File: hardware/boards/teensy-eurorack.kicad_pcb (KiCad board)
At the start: 2 copper layers, 118.1 x 101.6 mm, 98 parts, among them J10 AudioJack3_SwitchTR, J27 Conn_01x02, J28 Conn_02x08_Odd_Even, J4 AudioJack3_SwitchTR, J5 AudioJack3_SwitchTR, J6 AudioJack3_SwitchTR, J7 AudioJack3_SwitchTR, J8 AudioJack3_SwitchTR, J9 AudioJack3_SwitchTR, U1 CS42448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

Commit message: pcboard: re-connect LRCLK to codec, move hole for sd-extender cable further away from teensy, and move usb B headers up to avoid collision with SD-extender
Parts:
- moved JUSBB1 10.8 mm to (195.6, 116.8)
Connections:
- J10 pad RN: (no net) -> Net-(J10-PadRN)
- J10 pad TN: (no net) -> Net-(J10-PadTN)
- J28 pad 13: (no net) -> Net-(J28-Pad13)
- J28 pad 14: (no net) -> Net-(J28-Pad14)
- J28 pad 15: (no net) -> Net-(J28-Pad15)
- J28 pad 16: (no net) -> Net-(J28-Pad16)
- J4 pad RN: (no net) -> Net-(J4-PadRN)
- J4 pad TN: (no net) -> Net-(J4-PadTN)
- J5 pad RN: (no net) -> Net-(J5-PadRN)
- J5 pad TN: (no net) -> Net-(J5-PadTN)
- J6 pad RN: (no net) -> Net-(J6-PadRN)
- J6 pad TN: (no net) -> Net-(J6-PadTN)
- JM1 pad 5: (no net) -> Net-(JM1-Pad5)
- JM1 pad 6: (no net) -> Net-(JM1-Pad6)
- JM1 pad 7: (no net) -> Net-(JM1-Pad7)
- U1 pad 11: (no net) -> Net-(U1-Pad11)
- U1 pad 12: (no net) -> Net-(U1-Pad12)
- U1 pad 19: GND -> /LRCLK
- U1 pad 20: (no net) -> Net-(U1-Pad20)
- U1 pad 21: (no net) -> Net-(U1-Pad21)
- U1 pad 25: (no net) -> Net-(U1-Pad25)
- U1 pad 28: (no net) -> Net-(U1-Pad28)
- U1 pad 29: (no net) -> Net-(U1-Pad29)
- U1 pad 32: (no net) -> Net-(U1-Pad32)
- U1 pad 33: (no net) -> Net-(U1-Pad33)
- U1 pad 35: (no net) -> Net-(U1-Pad35)
- U1 pad 37: (no net) -> Net-(U1-Pad37)
- U1 pad 38: (no net) -> Net-(U1-Pad38)
- U1 pad 41: (no net) -> Net-(U1-Pad41)
- U1 pad 5: GND -> /LRCLK
- U1 pad 57: (no net) -> Net-(U1-Pad57)
- U1 pad 59: (no net) -> Net-(U1-Pad59)
- U1 pad 61: (no net) -> Net-(U1-Pad61)
- U4 pad 15: (no net) -> Net-(U4-Pad15)
- U4 pad 24: (no net) -> Net-(U4-Pad24)
- U4 pad 25: (no net) -> Net-(U4-Pad25)
- U4 pad 27: (no net) -> Net-(U4-Pad27)
- U4 pad 30: (no net) -> Net-(U4-Pad30)
- U4 pad 31: (no net) -> Net-(U4-Pad31)
- U4 pad 32: (no net) -> Net-(U4-Pad32)
- U4 pad 42: (no net) -> /LRCLK
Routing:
- net /LRCLK: track 0.00 -> 98.8 mm, vias 0 -> 2
- net Net-(JMUSBB1-Pad3): track 93.6 -> 80.1 mm
- net Net-(JMUSBB1-Pad4): track 96.6 -> 84.9 mm
- net Net-(JMUSBB1-Pad2): track 92.7 -> 82.0 mm
- net Net-(J27-Pad2): track 17.9 -> 21.6 mm
- net +3V3: track 277.0 -> 274.1 mm, vias 8 -> 9
- net /BCLK: track 85.3 -> 86.9 mm
- net /SDA: track 72.2 -> 71.1 mm
- net /SCL: track 73.2 -> 72.4 mm
- net /MCLK: track 79.7 -> 80.2 mm
- net /TDM_OUT: track 68.7 -> 68.2 mm
- net GND: track 145.8 -> 146.0 mm, vias 88 -> 98
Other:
- outline, holes or cut-outs redrawn
- board text added: "Teensy eurorack audio shield 9 Aug 2020 v1.9.1b"
- board text added: "https://github.com/newdigate/teensy-eurorack version 1.9.1b"
- board text removed: "Teensy eurorack audio shield 26 July 2020 v1.9.1"
- board text removed: "https://github.com/newdigate/teensy-eurorack version 1.9.1"

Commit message: silkscreen improvements
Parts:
- FB1: value Ferrite_Bead -> 220
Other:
- board text added: "Eurorack power bus"
- board text added: "USB device connection (to host) using female USB-B socket on front panel"
- board text added: "USB host connection using USB-A female socket on front panel"
- board text added: "connect jumper J27 to power from eurorack power bus 5v CAUTION: Do not connect teensy to host while using eurorack power."
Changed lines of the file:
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@@
   (general
     (thickness 1.6)
-    (drawings 23)
+    (drawings 35)
     (tracks 1524)
     (zones 0)
@@
   )
   (setup
-    (last_trace_width 0.4064)
+    (last_trace_width 0.2286)
     (user_trace_width 0.1524)
     (user_trace_width 0.2286)
@@
     (descr "Through hole straight pin header, 1x04, 2.54mm pitch, single row")
     (tags "Through hole pin header THT 1x04 2.54mm single row")
-    (fp_text reference JUSBB1 (at 0 2.33 -90) (layer B.SilkS)
+    (fp_text reference JUSBB1 (at 0 2.33 -90) (layer B.SilkS) hide
       (effects (font (size 1 1) (thickness 0.15)) (justify mirror))
     )
@@
     (descr "Through hole straight pin header, 2x08, 2.54mm pitch, double rows")
     (tags "Through hole pin header THT 2x08 2.54mm double row")
-    (fp_text reference J28 (at 1.27 2.33) (layer B.SilkS)
+    (fp_text reference J28 (at 1.27 -20.193) (layer B.SilkS)
       (effects (font (size 1 1) (thickness 0.15)) (justify mirror))
     )
@@
     (descr "Through hole straight pin header, 1x04, 2.54mm pitch, single row")
     (tags "Through hole pin header THT 1x04 2.54mm single row")
-    (fp_text reference JUSBA1 (at 0 2.33 270) (layer B.SilkS)
+    (fp_text reference JUSBA1 (at 0 2.33 270) (layer B.SilkS) hide
       (effects (font (size 1 1) (thickness 0.15)) (justify mirror))
     )
@@
     (descr "Through hole straight pin header, 1x02, 2.54mm pitch, single row")
     (tags "Through hole pin header THT 1x02 2.54mm single row")
-    (fp_text reference J27 (at 0 2.33) (layer B.SilkS)
+    (fp_text reference J27 (at 0 -5.08) (layer B.SilkS)
       (effects (font (size 1 1) (thickness 0.15)) (justify mirror))
     )
@@
     (tags inductor)
     (attr smd)
-    (fp_text reference FB1 (at 0 1.43) (layer B.SilkS)
+    (fp_text reference FB1 (at 0 -1.524) (layer B.SilkS)
       (effects (font (size 1 1) (thickness 0.15)) (justify mirror))
     )
-    (fp_text value Ferrite_Bead (at 0 -1.43) (layer B.Fab)
+    (fp_text value 220 (at 0 -2.794) (layer B.SilkS)
       (effects (font (size 1 1) (thickness 0.15)) (justify mirror))
     )
@@
     (fp_line (start 1.48 0.73) (end 1.48 -0.73) (layer B.CrtYd) (width 0.05))
     (fp_line (start 1.48 -0.73) (end -1.48 -0.73) (layer B.CrtYd) (width 0.05))
-    (fp_text user %R (at 0 0) (layer B.Fab)
+    (fp_text user %R (at 0 0) (layer B.SilkS) hide
       (effects (font (size 0.4 0.4) (thickness 0.06)) (justify mirror))
     )
@@
       (net 13 +5V))
   )
+  (gr_line (start 187.706 130.302) (end 188.214 130.302) (layer B.SilkS) (width 0.15))
+  (gr_line (start 188.214 131.064) (end 187.706 130.302) (layer B.SilkS) (width 0.15))
+  (gr_line (start 188.214 130.302) (end 188.214 131.064) (layer B.SilkS) (width 0.15))
+  (gr_line (start 188.722 130.302) (end 188.214 130.302) (layer B.SilkS) (width 0.15))
+  (gr_line (start 188.214 131.064) (end 188.722 130.302) (layer B.SilkS) (width 0.15))
+  (gr_line (start 188.214 125.73) (end 188.214 131.064) (layer B.SilkS) (width 0.15))
+  (gr_line (start 187.452 124.968) (end 188.214 125.73) (layer B.SilkS) (width 0.15))
+  (gr_text "USB host connection\nusing USB-A female socket\non front panel" (at 101.854 98.298) (layer B.SilkS)
+    (effects (font (size 1 1) (thickness 0.15)) (justify right mirror))
+  )
+  (gr_line (start 198.374 144.272) (end 209.296 144.272) (layer B.SilkS) (width 0.6096))
+  (gr_text "Eurorack power bus" (at 206.502 136.144 270) (layer B.SilkS)
+    (effects (font (size 1 1) (thickness 0.15)) (justify mirror))
+  )
+  (gr_text "USB device connection\n(to host) using female \nUSB-B socket on front panel" (at 185.928 115.57) (layer B.SilkS)
+    (effects (font (size 1 1) (thickness 0.15)) (justify left mirror))
+  )
+  (gr_text "connect jumper J27 \nto power from eurorack \npower bus 5v\n\nCAUTION: \nDo not connect \nteensy to host \nwhile using \neurorack power." (at 186.944 129.794) (layer B.SilkS)
+    (effects (font (size 0.762 0.762) (thickness 0.127)) (justify left mirror))
+  )
   (gr_text "https://github.com/newdigate/teensy-eurorack\nversion 1.9.1b" (at 109.22 119.38) (layer B.SilkS)
     (effects (font (size 1 1) (thickness 0.15)) (justify right mirror))
@@
     (effects (font (size 1.5 1.5) (thickness 0.3)) (justify mirror))
   )
-  (gr_text "USB B" (at 186.309 124.079) (layer B.SilkS)
+  (gr_text "USB B" (at 190.373 113.919) (layer B.SilkS)
     (effects (font (size 1.5 1.5) (thickness 0.3)) (justify mirror))
   )
-  (gr_text VCC (at 184.023 130.766286 270) (layer B.SilkS)
+  (gr_text VCC (at 188.087 120.606286 270) (layer B.SilkS)
     (effects (font (size 1.5 1.5) (thickness 0.3)) (justify mirror))
   )
-  (gr_text D- (at 186.436 130.302 270) (layer B.SilkS)
+  (gr_text D- (at 190.5 120.142 270) (layer B.SilkS)
     (effects (font (size 1.5 1.5) (thickness 0.3)) (justify mirror))
   )
-  (gr_text D+ (at 188.976 130.302 270) (layer B.SilkS)
+  (gr_text D+ (at 193.04 120.142 270) (layer B.SilkS)
     (effects (font (size 1.5 1.5) (thickness 0.3)) (justify mirror))
   )

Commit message: via sizes corrected
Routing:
- net /TFT_SCK: track 98.0 -> 96.5 mm, vias 6 -> 5
- net /ADC_SCK: track 119.6 -> 120.8 mm
- net /DAC_SYNC: track 130.6 -> 131.2 mm
- net /DAC_SDOUT: track 120.7 -> 121.3 mm
- net /AGND: vias 55 -> 43
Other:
- net class Default: via_dia 0.8 -> 0.3556; via_drill 0.4 -> 0.2032
- rule via_min_drill: 0.1143 -> 0.2032
- rule via_min_size: 0.2286 -> 0.3556

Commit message: schematic, pcb changes for v2.0
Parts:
- FB1: value 220 -> Ferrite_Bead
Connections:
- net /ADC_SCK renamed /ADC_RANGE
- J10 pad RN: Net-(J10-PadRN) -> (no net)
- J10 pad TN: Net-(J10-PadTN) -> (no net)
- J28 pad 13: Net-(J28-Pad13) -> (no net)
- J28 pad 14: Net-(J28-Pad14) -> (no net)
- J28 pad 15: Net-(J28-Pad15) -> (no net)
- J28 pad 16: Net-(J28-Pad16) -> (no net)
- J4 pad RN: Net-(J4-PadRN) -> (no net)
- J4 pad TN: Net-(J4-PadTN) -> (no net)
- J5 pad RN: Net-(J5-PadRN) -> (no net)
- J5 pad TN: Net-(J5-PadTN) -> (no net)
- J6 pad RN: Net-(J6-PadRN) -> (no net)
- J6 pad TN: Net-(J6-PadTN) -> (no net)
- JM1 pad 5: Net-(JM1-Pad5) -> GND
- JM1 pad 6: Net-(JM1-Pad6) -> /ADC_RESET
- JM1 pad 7: Net-(JM1-Pad7) -> GND
- JM2 pad 13: +12V -> (no net)
- JM2 pad 14: -12V -> (no net)
- JM2 pad 7: /DAC_SDOUT -> GND
- U1 pad 11: Net-(U1-Pad11) -> (no net)
- U1 pad 12: Net-(U1-Pad12) -> (no net)
- U1 pad 20: Net-(U1-Pad20) -> (no net)
- U1 pad 21: Net-(U1-Pad21) -> (no net)
- U1 pad 25: Net-(U1-Pad25) -> (no net)
- U1 pad 28: Net-(U1-Pad28) -> (no net)
- U1 pad 29: Net-(U1-Pad29) -> (no net)
- U1 pad 32: Net-(U1-Pad32) -> (no net)
- U1 pad 33: Net-(U1-Pad33) -> (no net)
- U1 pad 35: Net-(U1-Pad35) -> (no net)
- U1 pad 37: Net-(U1-Pad37) -> (no net)
- U1 pad 38: Net-(U1-Pad38) -> (no net)
- U1 pad 41: Net-(U1-Pad41) -> (no net)
- U1 pad 57: Net-(U1-Pad57) -> (no net)
- U1 pad 59: Net-(U1-Pad59) -> (no net)
- U1 pad 61: Net-(U1-Pad61) -> (no net)
- U4 pad 15: Net-(U4-Pad15) -> (no net)
- U4 pad 24: Net-(U4-Pad24) -> (no net)
- U4 pad 25: Net-(U4-Pad25) -> (no net)
- U4 pad 26: /ADC_MISO -> (no net)
- U4 pad 27: Net-(U4-Pad27) -> /ADC_RESET
- U4 pad 30: Net-(U4-Pad30) -> /DAC_SYNC
- U4 pad 31: Net-(U4-Pad31) -> /ADC_MISO
- U4 pad 32: Net-(U4-Pad32) -> (no net)
- U4 pad 33: /DAC_SDOUT -> (no net)
- U4 pad 38: /DAC_SYNC -> (no net)
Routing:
- net /DAC_SDOUT: track 121.3 -> 0.00 mm, vias 5 -> 0
- net /ADC_RESET: track 0.00 -> 111.6 mm, vias 0 -> 5
- net -12V: track 242.0 -> 175.3 mm
- net +12V: track 252.8 -> 191.0 mm
- net /DAC_SYNC: track 131.2 -> 105.2 mm, vias 5 -> 1
- net GND: track 146.0 -> 155.9 mm, vias 98 -> 239
- net /TFT_DC: track 120.7 -> 124.9 mm
- net /ADC_MISO: track 127.0 -> 123.4 mm, vias 0 -> 1
- net /ADC_BUSY: track 136.4 -> 134.7 mm
- net /TFT_MOSI: track 102.2 -> 103.4 mm
- net +5V: track 221.8 -> 221.3 mm
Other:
- board text added: "Teensy eurorack audio shield 6 Nov 2020 v2.0"
- board text added: "https://github.com/newdigate/teensy-eurorack version 2.0"
- board text removed: "Teensy eurorack audio shield 9 Aug 2020 v1.9.1b"
- board text removed: "https://github.com/newdigate/teensy-eurorack version 1.9.1b"

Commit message: mainboard: removed loopback for SPI clock as no longer needed
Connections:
- U4 pad 23: /DAC_SCK -> (no net)
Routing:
- net /DAC_SCK: track 84.4 -> 71.8 mm, vias 2 -> 1

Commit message: Breakout: changed from 4 layer to 2 layer; Mainboard: add serial daisy chain RX/TX to RX4/TX4
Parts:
- added JDAISYM1: Conn_01x03, Connector_PinHeader_2.54mm:PinHeader_1x03_P2.54mm_Vertical, B.Cu at (112.5, 105.6)
- added JDAISYS1: Conn_01x03, Connector_PinHeader_2.54mm:PinHeader_1x03_P2.54mm_Vertical, B.Cu at (117.7, 105.5)
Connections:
- J10 pad RN: (no net) -> Net-(J10-PadRN)
- J10 pad TN: (no net) -> Net-(J10-PadTN)
- J28 pad 13: (no net) -> Net-(J28-Pad13)
- J28 pad 14: (no net) -> Net-(J28-Pad14)
- J28 pad 15: (no net) -> Net-(J28-Pad15)
- J28 pad 16: (no net) -> Net-(J28-Pad16)
- J4 pad RN: (no net) -> Net-(J4-PadRN)
- J4 pad TN: (no net) -> Net-(J4-PadTN)
- J5 pad RN: (no net) -> Net-(J5-PadRN)
- J5 pad TN: (no net) -> Net-(J5-PadTN)
- J6 pad RN: (no net) -> Net-(J6-PadRN)
- J6 pad TN: (no net) -> Net-(J6-PadTN)
- JM2 pad 13: (no net) -> Net-(JM2-Pad13)
- JM2 pad 14: (no net) -> Net-(JM2-Pad14)
- U1 pad 11: (no net) -> Net-(U1-Pad11)
- U1 pad 12: (no net) -> Net-(U1-Pad12)
- U1 pad 20: (no net) -> Net-(U1-Pad20)
- U1 pad 21: (no net) -> Net-(U1-Pad21)
- U1 pad 25: (no net) -> Net-(U1-Pad25)
- U1 pad 28: (no net) -> Net-(U1-Pad28)
- U1 pad 29: (no net) -> Net-(U1-Pad29)
- U1 pad 32: (no net) -> Net-(U1-Pad32)
- U1 pad 33: (no net) -> Net-(U1-Pad33)
- U1 pad 35: (no net) -> Net-(U1-Pad35)
- U1 pad 37: (no net) -> Net-(U1-Pad37)
- U1 pad 38: (no net) -> Net-(U1-Pad38)
- U1 pad 41: (no net) -> Net-(U1-Pad41)
- U1 pad 57: (no net) -> Net-(U1-Pad57)
- U1 pad 59: (no net) -> Net-(U1-Pad59)
- U1 pad 61: (no net) -> Net-(U1-Pad61)
- U4 pad 15: (no net) -> Net-(U4-Pad15)
- U4 pad 23: (no net) -> Net-(U4-Pad23)
- U4 pad 24: (no net) -> Net-(U4-Pad24)
- U4 pad 25: (no net) -> Net-(U4-Pad25)
- U4 pad 26: (no net) -> Net-(U4-Pad26)
- U4 pad 32: (no net) -> Net-(U4-Pad32)
- U4 pad 33: (no net) -> /P3
- U4 pad 38: (no net) -> /D_RX
- U4 pad 39: /P3 -> /D_TX
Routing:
- net /D_RX: track 0.00 -> 64.9 mm
- net /D_TX: track 0.00 -> 59.0 mm
- net /ADC_MISO: track 123.4 -> 111.1 mm
- net /P3: track 5.50 -> 15.6 mm, vias 0 -> 1
- net /ES3: track 23.1 -> 24.5 mm
- net /ADC_RESET: track 111.6 -> 110.8 mm
- net /P2: track 19.9 -> 20.5 mm
- net GND: vias 239 -> 270
- net /P4: vias 6 -> 4
- net /SDA: vias 3 -> 4
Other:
- board text added: "MASTER RX"
- board text added: "MASTER TX"
- board text added: "SLAVE RX"
- board text added: "SLAVE TX"
- board text added: "Serial Daisy Chain"
- board text added: "Teensy eurorack audio shield 27 Jan 2021 v2.0.1"
- board text added: "https://github.com/newdigate/teensy-eurorack version 2.0.1"
- board text removed: "Teensy eurorack audio shield 6 Nov 2020 v2.0"
- board text removed: "https://github.com/newdigate/teensy-eurorack version 2.0"

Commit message: mainboard pcb: spaced tracks out
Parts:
- moved JUSBB1 3.37 mm to (195.6, 120.2)
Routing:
- net /AGND: track 258.4 -> 308.6 mm
- net /ADC_CONVST: track 283.1 -> 251.2 mm
- net GND: track 155.9 -> 133.9 mm, vias 270 -> 167
- net /TFT_MOSI: track 103.4 -> 84.8 mm, vias 1 -> 3
- net /MIDI_RX: track 123.7 -> 132.3 mm, vias 1 -> 2
- net Net-(JMUSBB1-Pad2): track 82.0 -> 90.2 mm
- net /DAC_SYNC: track 105.2 -> 97.3 mm
- net /ADC_CS: track 114.2 -> 107.1 mm
- net /ADC_BUSY: track 134.7 -> 128.6 mm
- net /TFT_DC: track 124.9 -> 119.5 mm
- net /ES1: track 79.7 -> 75.0 mm, vias 6 -> 5
- net /SCL: track 72.0 -> 67.4 mm
- net /sheet5F0E4EAE/LEFT: track 37.3 -> 41.8 mm
- net /sheet5F0E4EAE/RIGHT: track 42.9 -> 47.2 mm
- net /SDA: track 71.0 -> 66.9 mm
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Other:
- board text added: "Teensy eurorack audio shield 30 Jan 2021 v2.0.2"
- board text added: "https://github.com/newdigate/teensy-eurorack version 2.0.2"
- board text removed: "Teensy eurorack audio shield 27 Jan 2021 v2.0.1"
- board text removed: "https://github.com/newdigate/teensy-eurorack version 2.0.1"

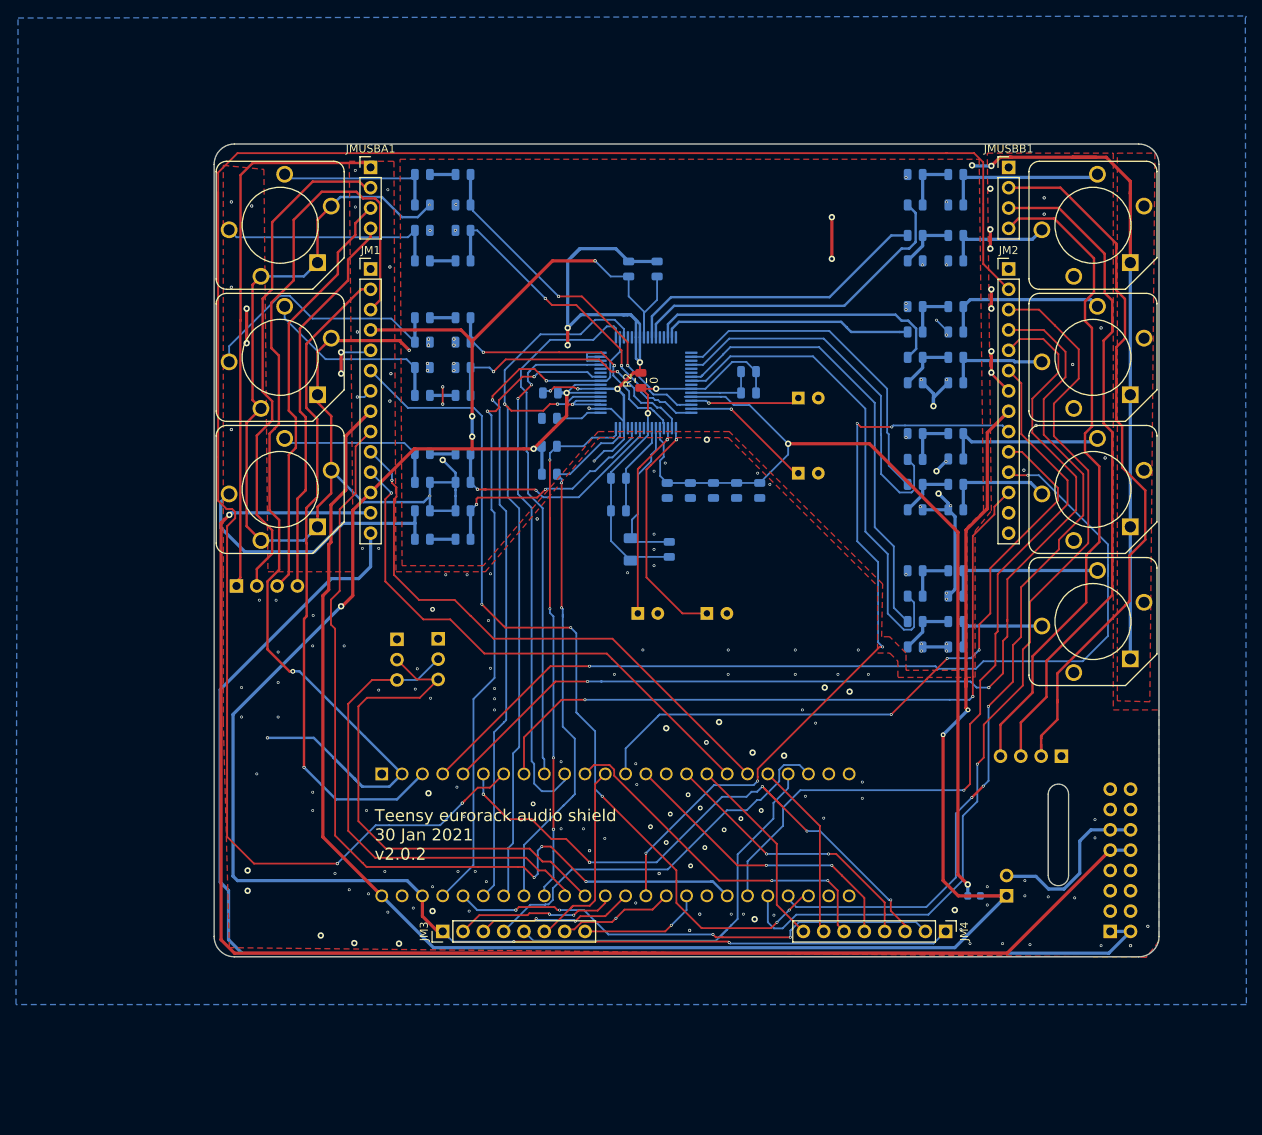
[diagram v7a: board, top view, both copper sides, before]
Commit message: mainboard pcb: minor cleanup
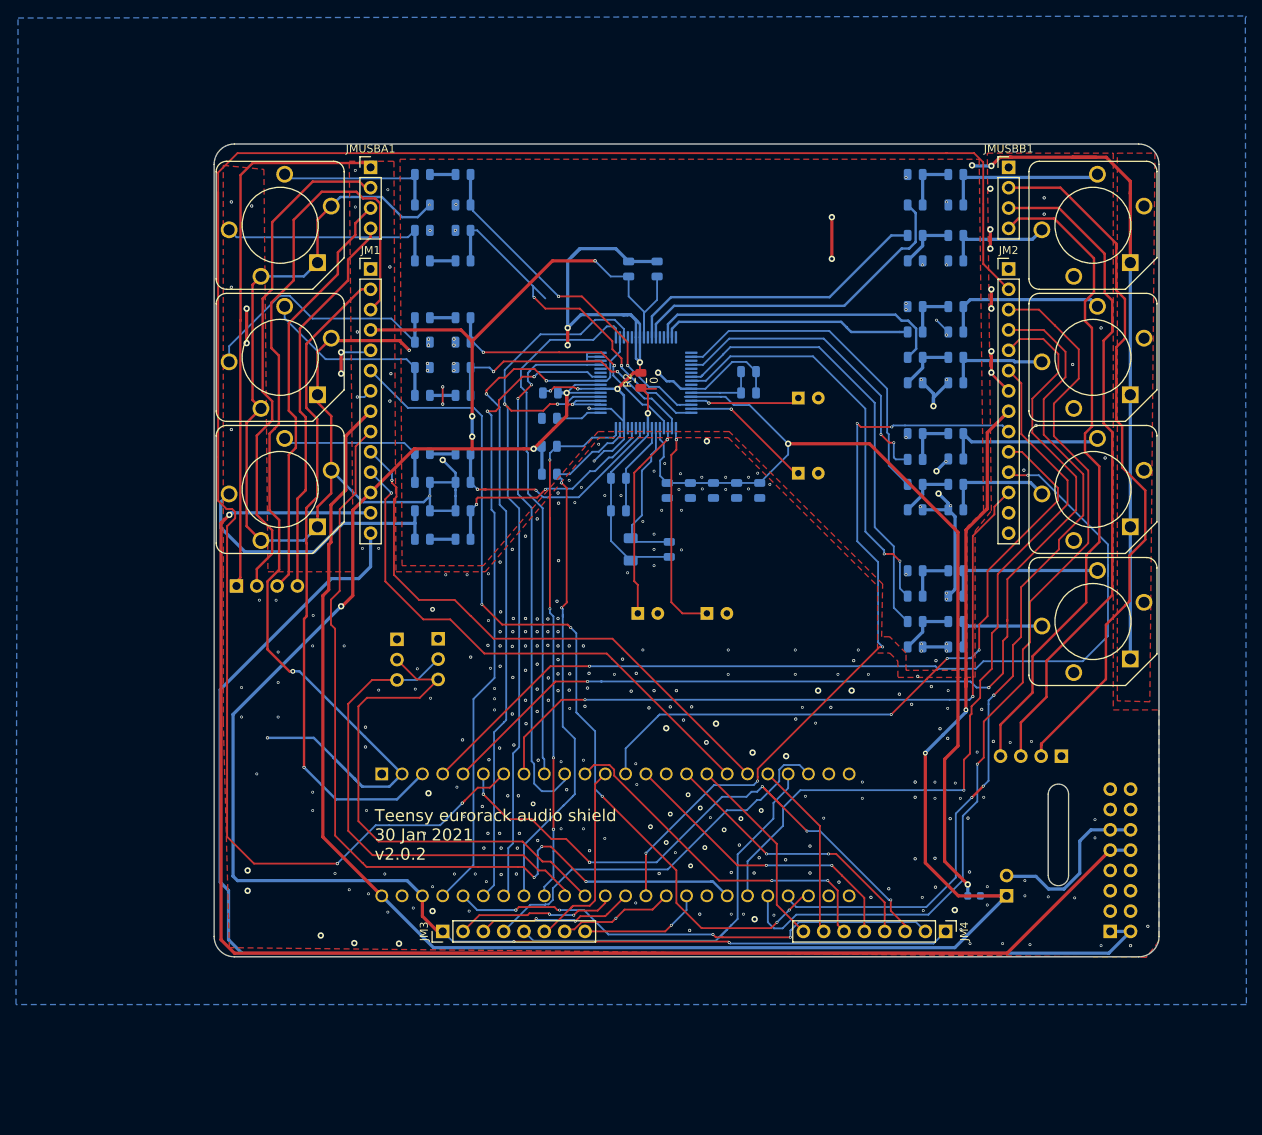
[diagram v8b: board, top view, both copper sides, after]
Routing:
- net /sheet5F0EA26B/RIGHT: track 61.7 -> 52.8 mm, vias 0 -> 2
- net /sheet5F0E4EAE/RIGHT: track 47.2 -> 38.6 mm, vias 0 -> 2
- net Net-(C3-Pad1): track 29.6 -> 27.1 mm
- net /AudioIn/RIGHT: track 42.5 -> 45.0 mm
- net /BCLK: track 87.6 -> 89.1 mm
- net Net-(C10-Pad1): track 112.7 -> 114.0 mm
- net +5V: track 224.5 -> 225.9 mm
- net /sheet5F6F72D7/LEFT: track 34.3 -> 33.5 mm
- net /AGND: track 308.6 -> 309.2 mm
- net /SCL: track 67.4 -> 68.0 mm
- net /sheet5F6F72D7/RIGHT: track 33.7 -> 33.1 mm
- net GND: vias 167 -> 309
